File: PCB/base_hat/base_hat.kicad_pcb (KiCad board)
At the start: 2 copper layers, 65 x 56 mm, 15 parts, among them M1 Fan_4pin, P1 Conn_02x20_Odd_Even, U1 DS3231MZ

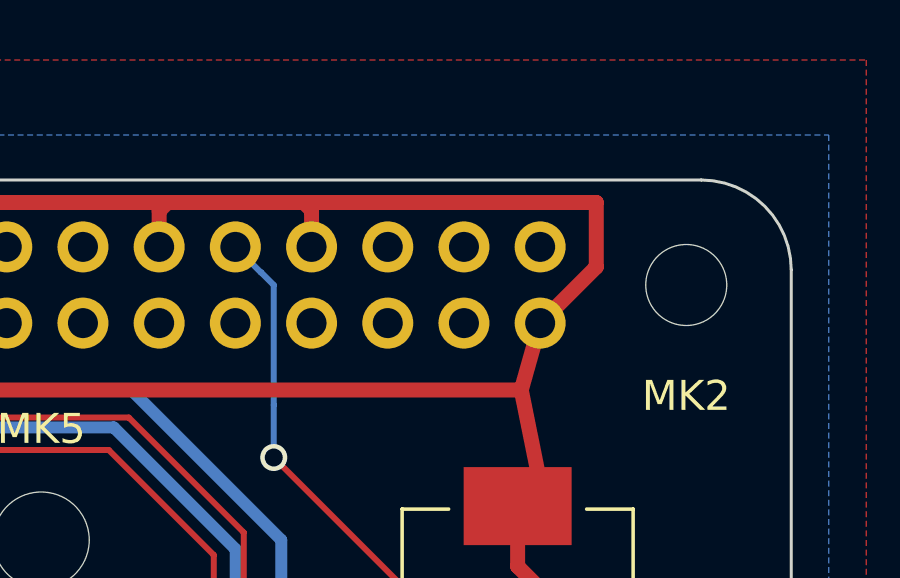
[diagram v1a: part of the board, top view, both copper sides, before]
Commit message: Add mounting holes isolation
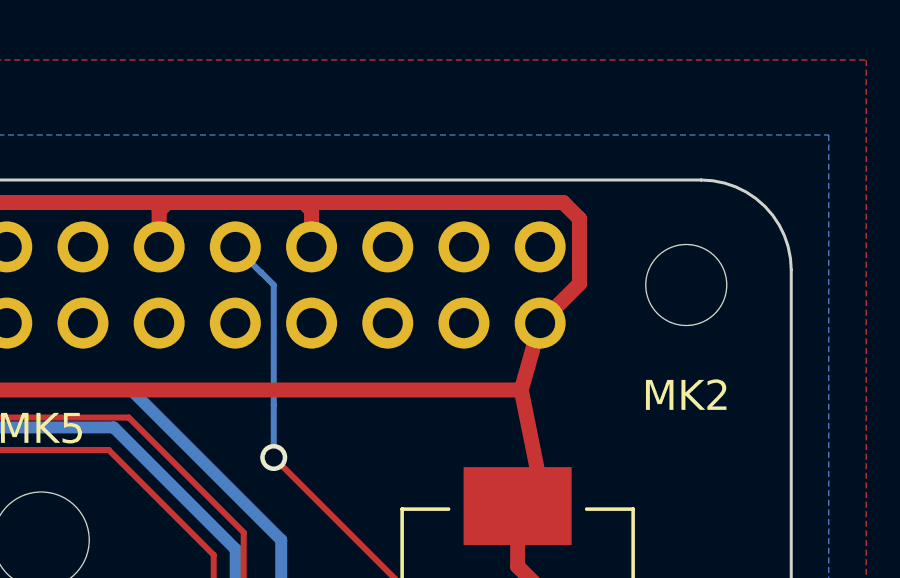
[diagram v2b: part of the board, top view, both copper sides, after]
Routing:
- net GND: track 191.8 -> 190.7 mm

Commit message: upgrade relais hat and all hat to kicad 7.0
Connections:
- net +3V3 renamed +3.3V
- M1 pad 3: (no net) -> unconnected-(M1-Tacho-Pad3)
- P1 pad 10: (no net) -> unconnected-(P1-Pin_10-Pad10)
- P1 pad 11: (no net) -> unconnected-(P1-Pin_11-Pad11)
- P1 pad 12: (no net) -> unconnected-(P1-Pin_12-Pad12)
- P1 pad 13: (no net) -> unconnected-(P1-Pin_13-Pad13)
- P1 pad 15: (no net) -> unconnected-(P1-Pin_15-Pad15)
- P1 pad 16: (no net) -> unconnected-(P1-Pin_16-Pad16)
- P1 pad 18: (no net) -> unconnected-(P1-Pin_18-Pad18)
- P1 pad 19: (no net) -> unconnected-(P1-Pin_19-Pad19)
- P1 pad 21: (no net) -> unconnected-(P1-Pin_21-Pad21)
- P1 pad 22: (no net) -> unconnected-(P1-Pin_22-Pad22)
- P1 pad 23: (no net) -> unconnected-(P1-Pin_23-Pad23)
- P1 pad 24: (no net) -> unconnected-(P1-Pin_24-Pad24)
- P1 pad 26: (no net) -> unconnected-(P1-Pin_26-Pad26)
- P1 pad 27: (no net) -> unconnected-(P1-Pin_27-Pad27)
- P1 pad 28: (no net) -> unconnected-(P1-Pin_28-Pad28)
- P1 pad 29: (no net) -> unconnected-(P1-Pin_29-Pad29)
- P1 pad 31: (no net) -> unconnected-(P1-Pin_31-Pad31)
- P1 pad 33: (no net) -> unconnected-(P1-Pin_33-Pad33)
- P1 pad 35: (no net) -> unconnected-(P1-Pin_35-Pad35)
- P1 pad 36: (no net) -> unconnected-(P1-Pin_36-Pad36)
- P1 pad 37: (no net) -> unconnected-(P1-Pin_37-Pad37)
- P1 pad 38: (no net) -> unconnected-(P1-Pin_38-Pad38)
- P1 pad 40: (no net) -> unconnected-(P1-Pin_40-Pad40)
- P1 pad 7: (no net) -> unconnected-(P1-Pin_7-Pad7)
- P1 pad 8: (no net) -> unconnected-(P1-Pin_8-Pad8)
- U1 pad 1: (no net) -> unconnected-(U1-32KHZ-Pad1)
- U1 pad 3: (no net) -> unconnected-(U1-~{INT}/SQW-Pad3)
- U1 pad 4: (no net) -> unconnected-(U1-~{RST}-Pad4)
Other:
- net class Default removed
- net class Power removed
